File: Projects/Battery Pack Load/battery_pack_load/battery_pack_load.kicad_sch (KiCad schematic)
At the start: 6 parts, among them Q1 2N3906, Q2 PN2222A

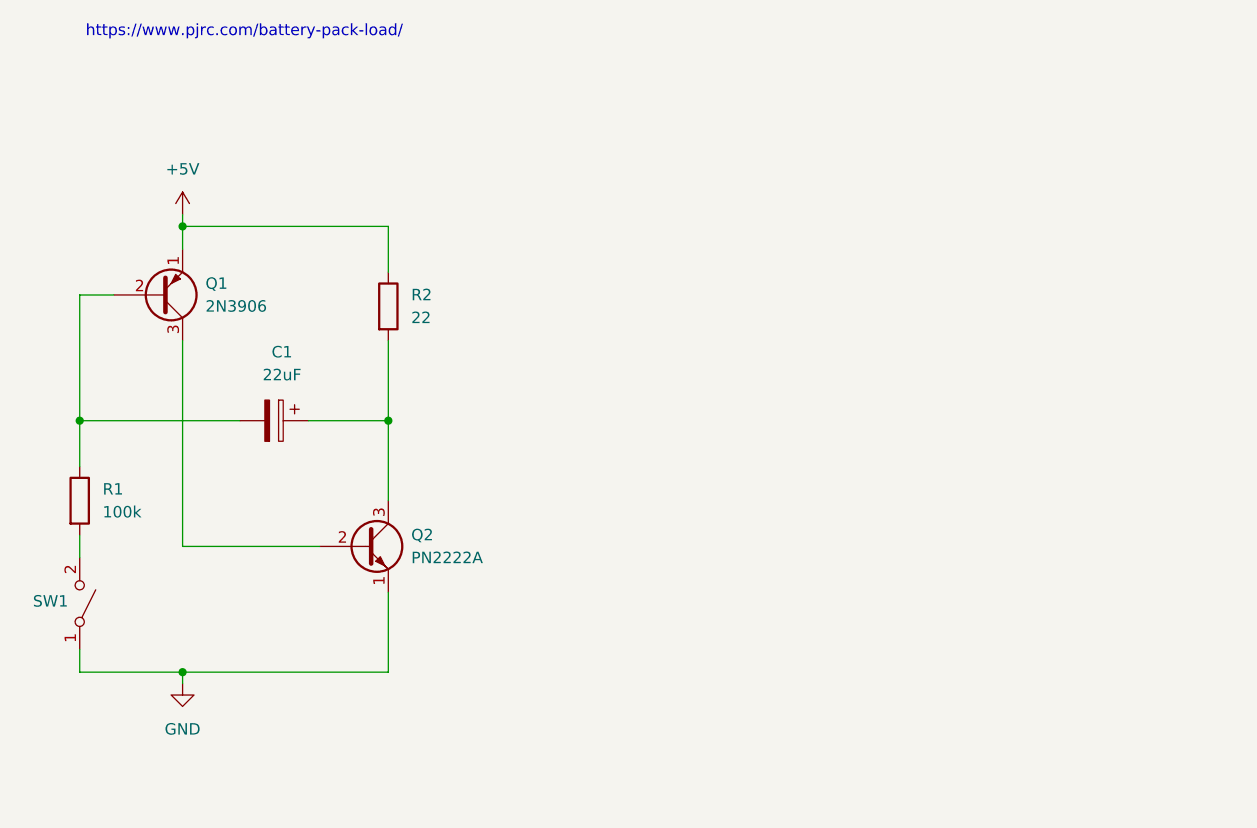
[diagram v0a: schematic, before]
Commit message: Updated battery pack load
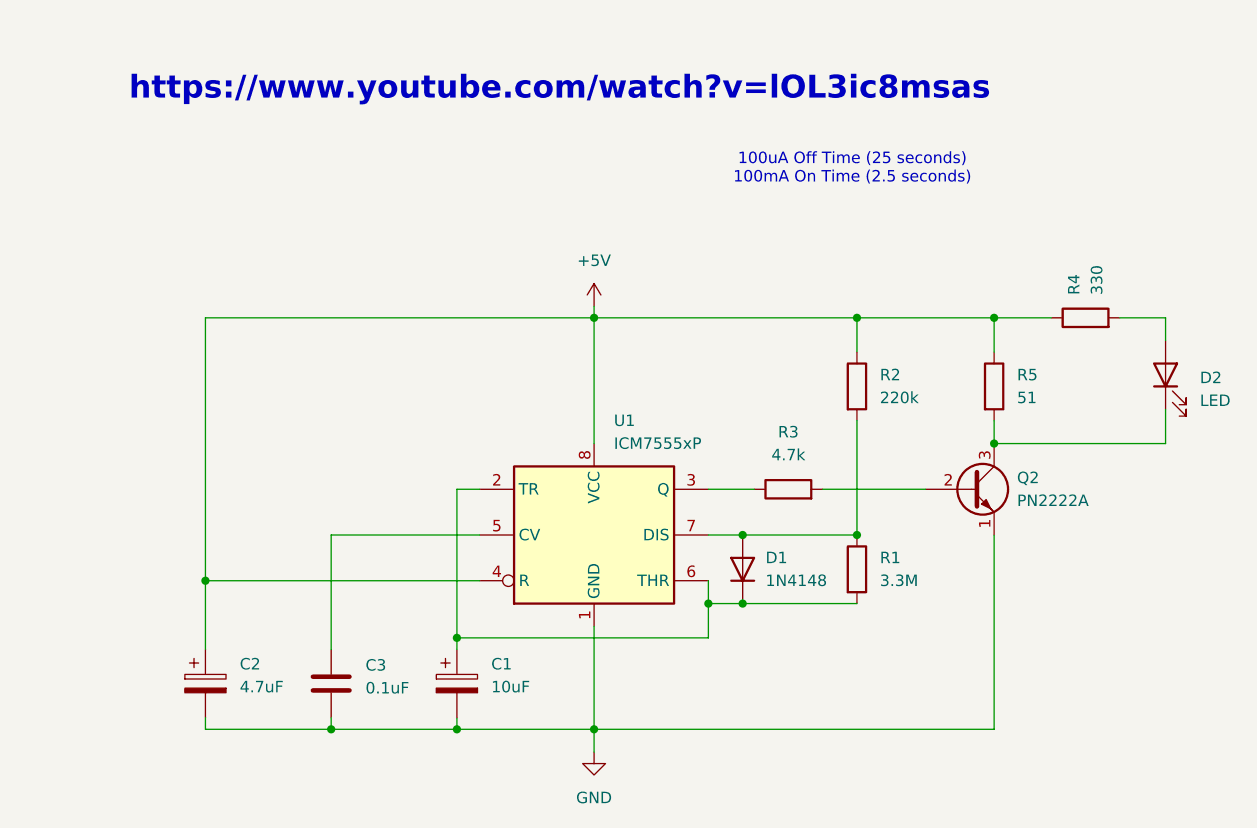
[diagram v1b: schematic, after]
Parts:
- removed Q1: 2N3906, Package_TO_SOT_THT:TO-92_Inline, symbol Transistor_BJT:2N3906
- removed SW1: ~, symbol Switch:SW_SPST
- added C2: 4.7uF, symbol Device:C_Polarized
- added C3: 0.1uF, symbol Device:C
- added D1: 1N4148, Diode_THT:D_DO-35_SOD27_P7.62mm_Horizontal, symbol Diode:1N4148
- added D2: LED, symbol Device:LED
- added R2: 220k, symbol Device:R
- added R4: 330, symbol Device:R
- added R5: 51, symbol Device:R
- added U1: ICM7555xP, Package_DIP:DIP-8_W7.62mm, symbol Timer:ICM7555xP
- C1: value 22uF -> 10uF
- R1: value 100k -> 3.3M
- R3: renamed from R2; value 22 -> 4.7k
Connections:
- net +5V: now also C2.1, R2.1, R4.1, R5.1, U1.4 (R), U1.8 (VCC); no longer R3.1
- net GND: now also C1.2, C2.2, C3.2, U1.1 (GND)
- net at R1.1: now also D1.2 (A), R2.2, U1.7 (DIS); no longer C1.2
- net at R1.2: now also C1.1, D1.1 (K), U1.2 (TR), U1.6 (THR)
- net at Q2.2 (B): now also R3.2
- new net: D2.2 (A), R4.2
- new net: C3.1, U1.5 (CV)
- new net: R3.1, U1.3 (Q)
- new net: D2.1 (K), Q2.3 (C), R5.2
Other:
- note added: "100uA Off Time (25 seconds) 100mA On Time (2.5 seconds)"
- note added: "https://www.youtube.com/watch?v=lOL3ic8msas"
- note removed: "https://www.pjrc.com/battery-pack-load/"
- moved on the sheet: C1, Q2, R1, R3
